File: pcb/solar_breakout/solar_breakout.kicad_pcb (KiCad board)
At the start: 2 copper layers, 21 parts, among them IC1 LTC3105, J1 CONN_01x02, J2 CONN_01x02, J3 CONN_01x02, J4 CONN_01x02, J5 CONN_01x02, J6 CONN_01x02

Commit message: Set up design rules
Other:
- rule pad_to_mask_clearance: 0.051 -> 0
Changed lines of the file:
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@@
     (pad_size 1.524 1.524)
     (pad_drill 0.762)
-    (pad_to_mask_clearance 0.051)
+    (pad_to_mask_clearance 0)
     (solder_mask_min_width 0.25)
     (aux_axis_origin 0 0)

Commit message: First draft of PCB
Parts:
- added REF**: SIL-254P-02, agg:SIL-254P-02, F.Cu at (154.9, 118.3)
- added REF**: SIL-254P-03, agg:SIL-254P-03, F.Cu at (142.1, 119.6)
- added REF**: SIL-254P-02, agg:SIL-254P-02, F.Cu at (158.8, 100.2)
- added REF**: SIL-254P-02, agg:SIL-254P-02, F.Cu at (143.6, 100.2)
- moved D2 154.7 mm to (142.2, 138.4), turned to 90 degrees
- moved J2 148.9 mm to (144.8, 111.1), turned to 270 degrees
- moved C7 146.6 mm to (153.0, 94.0), turned to 180 degrees
- moved L1 145.9 mm to (154.9, 125.7)
- moved J4 144.7 mm to (157.5, 138.4), turned to 270 degrees
- moved IC1 142.9 mm to (149.9, 119.4)
- moved C3 142.8 mm to (153.7, 133.3), turned to 180 degrees
- moved J1 140.1 mm to (149.9, 138.4), turned to 270 degrees
- moved C2 139.8 mm to (147.3, 142.2)
- moved D3 138.2 mm to (142.2, 108.0), turned to 270 degrees
- moved J5 136.4 mm to (149.9, 125.1), turned to 270 degrees
- moved J6 128.5 mm to (163.2, 118.1), turned to 270 degrees
- moved C5 126.8 mm to (146.7, 119.4), turned to 270 degrees
- moved R4 118.7 mm to (154.9, 109.9), turned to 90 degrees
- moved C4 118.0 mm to (146.1, 101.6), turned to 90 degrees
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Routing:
- net /Cap_V: track 0.00 -> 77.3 mm
- net /Panel_V: track 0.00 -> 50.0 mm
- net Net-(C4-Pad1): track 0.00 -> 38.9 mm
- net Net-(IC1-Pad5): track 0.00 -> 26.4 mm
- net Net-(C3-Pad1): track 0.00 -> 22.6 mm
- net Net-(IC1-Pad7): track 0.00 -> 10.1 mm
- net /Array_1_+: track 0.00 -> 7.92 mm
- net /D_anode: track 0.00 -> 5.78 mm
- net /Array_2_+: track 0.00 -> 2.58 mm
- net Net-(C5-Pad1): track 0.00 -> 1.77 mm

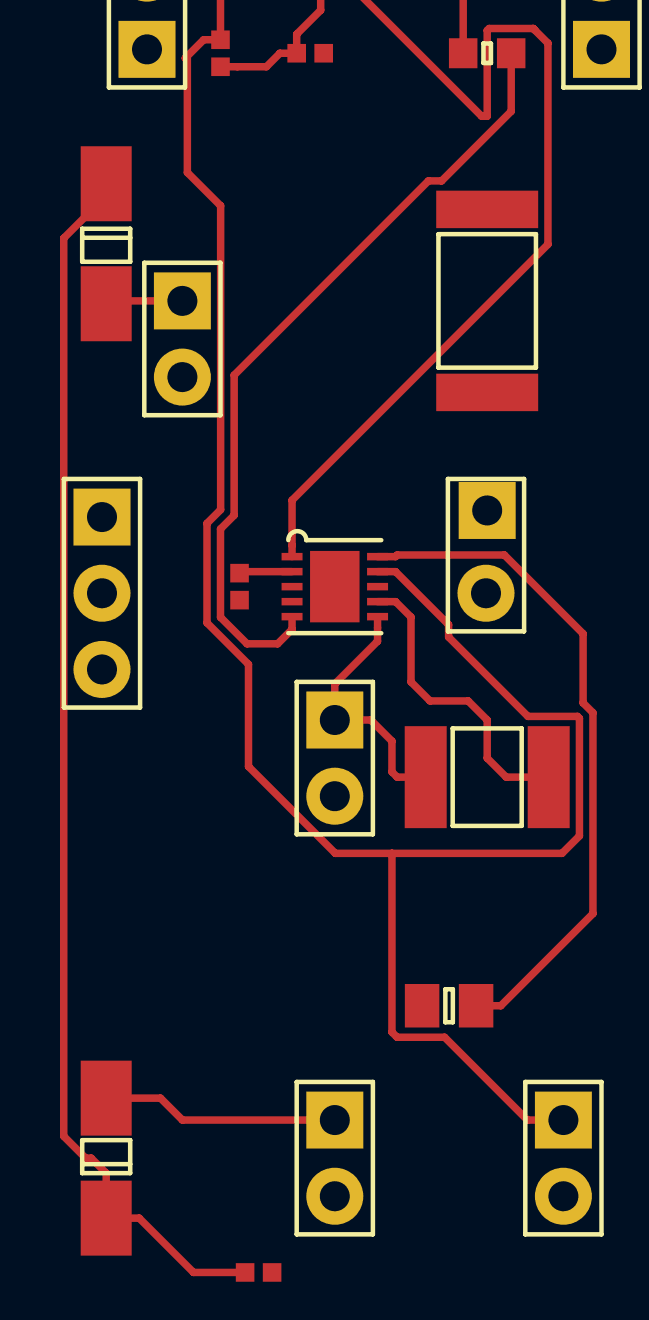
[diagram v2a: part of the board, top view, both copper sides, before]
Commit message: Fix some stuff on pcb (from the Dyson Centre)
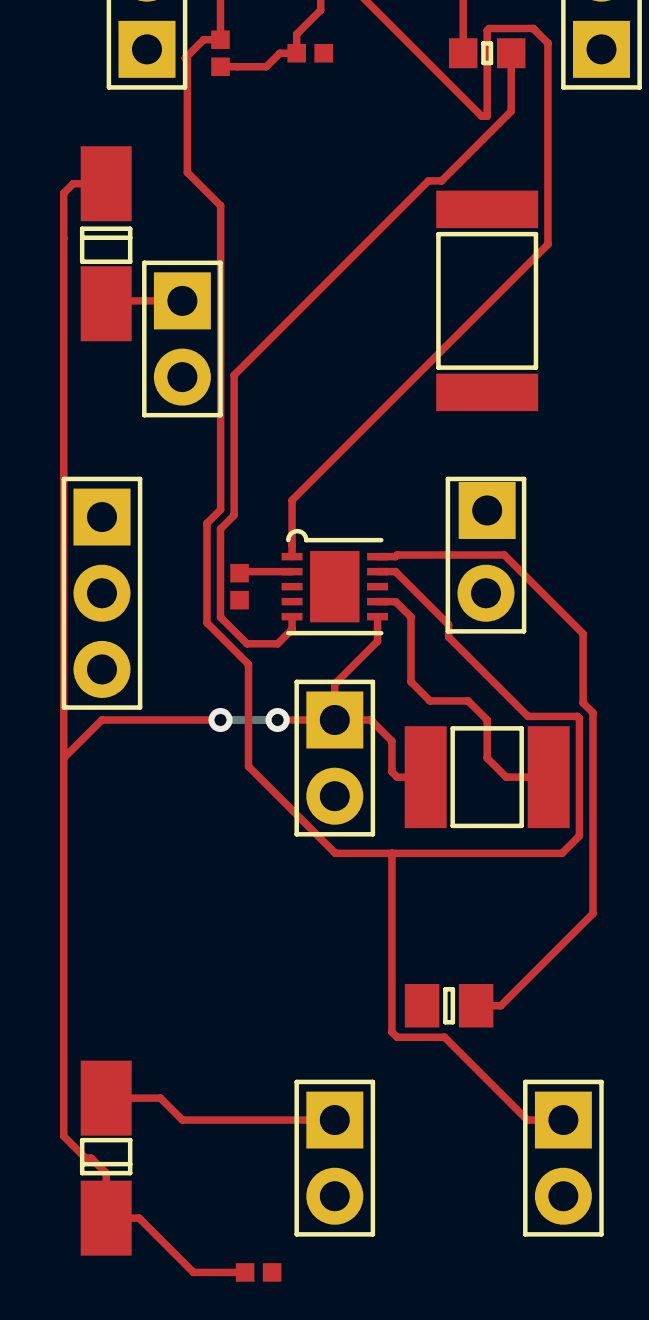
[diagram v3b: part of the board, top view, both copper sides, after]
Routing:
- net /Panel_V: track 50.0 -> 60.6 mm, vias 0 -> 2
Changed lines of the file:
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@@
-(kicad_pcb (version 20171130) (host pcbnew "(6.0.0-rc1-dev-1613-ga55d9819b)")
+(kicad_pcb (version 4) (host pcbnew 4.0.1-stable)
   (general
+    (links 37)
+    (no_connects 17)
+    (area 138.250714 90.315 166.483095 143.919762)
     (thickness 1.6)
     (drawings 0)
-    (tracks 115)
+    (tracks 124)
     (zones 0)
     (modules 25)
@@
     (zone_45_only no)
     (trace_min 0.2)
+    (segment_width 0.2)
+    (edge_width 0.05)
     (via_size 0.8)
     (via_drill 0.4)
@@
     (uvia_min_size 0.2)
     (uvia_min_drill 0.1)
-    (edge_width 0.05)
-    (segment_width 0.2)
     (pcb_text_width 0.3)
     (pcb_text_size 1.5 1.5)
@@
       (layerselection 0x010fc_ffffffff)
       (usegerberextensions false)
-      (usegerberattributes false)
-      (usegerberadvancedattributes false)
-      (creategerberjobfile false)
       (excludeedgelayer true)
       (linewidth 0.100000)
@@
       (hpglpennumber 1)
       (hpglpenspeed 20)
-      (hpglpendiameter 15.000000)
+      (hpglpendiameter 15)
+      (hpglpenoverlay 2)
       (psnegative false)
       (psa4output false)
@@
   (module agg:0402 (layer F.Cu)
     (at 146.685 119.38 270)
-    (fp_text reference C5 (at -1.71 0) (layer F.Fab)
-      (effects (font (size 1 1) (thickness 0.15)))
-    )
-    (fp_text value 4.7u (at 1.71 0) (layer F.Fab)
+    (fp_text reference C5 (at -1.71 0 360) (layer F.Fab)
+      (effects (font (size 1 1) (thickness 0.15)))
+    )
+    (fp_text value 4.7u (at 1.71 0 360) (layer F.Fab)
       (effects (font (size 1 1) (thickness 0.15)))
     )
@@
   (module jerboa:SMA_DIODE (layer F.Cu)
     (at 142.24 107.95 270)
-    (fp_text reference D3 (at -4 0) (layer F.Fab)
-      (effects (font (size 1 1) (thickness 0.15)))
-    )
-    (fp_text value SCHOTTKY (at 4.1 0) (layer F.Fab)
+    (fp_text reference D3 (at -4 0 360) (layer F.Fab)
+      (effects (font (size 1 1) (thickness 0.15)))
+    )
+    (fp_text value SCHOTTKY (at 4.1 0 360) (layer F.Fab)
       (effects (font (size 1 1) (thickness 0.15)))
     )
@@
   (segment (start 154.305 97.155) (end 155.575 97.155) (width 0.25) (layer F.Cu) (net 1))
   (segment (start 154.14 97.32) (end 154.305 97.155) (width 0.25) (layer F.Cu) (net 1))
+  (segment (start 142.24 105.95) (end 141.14 105.95) (width 0.25) (layer F.Cu) (net 3))
+  (segment (start 141.14 105.95) (end 140.824999 106.265001) (width 0.25) (layer F.Cu) (net 3))
+  (segment (start 140.824999 106.265001) (end 140.824999 107.765001) (width 0.25) (layer F.Cu) (net 3))
+  (segment (start 140.824999 107.765001) (end 140.824999 125.095) (width 0.25) (layer F.Cu) (net 3))
+  (segment (start 140.824999 125.095) (end 140.824999 137.700001) (width 0.25) (layer F.Cu) (net 3))
+  (segment (start 146.05 123.825) (end 142.094999 123.825) (width 0.25) (layer F.Cu) (net 3))
+  (segment (start 142.094999 123.825) (end 140.824999 125.095) (width 0.25) (layer F.Cu) (net 3))
+  (segment (start 147.955 123.825) (end 146.05 123.825) (width 0.25) (layer B.Cu) (net 3))
+  (via (at 146.05 123.825) (size 0.8) (drill 0.4) (layers F.Cu B.Cu) (net 3))
+  (segment (start 149.86 123.825) (end 147.955 123.825) (width 0.25) (layer F.Cu) (net 3))
+  (via (at 147.955 123.825) (size 0.8) (drill 0.4) (layers F.Cu B.Cu) (net 3))
   (segment (start 143.34 140.43) (end 142.24 140.43) (width 0.25) (layer F.Cu) (net 3))
   (segment (start 145.15 142.24) (end 143.34 140.43) (width 0.25) (layer F.Cu) (net 3))
@@
   (segment (start 142.24 138.93) (end 142.24 140.43) (width 0.25) (layer F.Cu) (net 3))
   (segment (start 142.24 105.95) (end 142.24 106.35) (width 0.25) (layer F.Cu) (net 3))
-  (segment (start 142.24 106.35) (end 140.824999 107.765001) (width 0.25) (layer F.Cu) (net 3))
-  (segment (start 140.824999 107.765001) (end 140.824999 137.700001) (width 0.25) (layer F.Cu) (net 3))
   (segment (start 140.824999 137.700001) (end 141.554998 138.43) (width 0.25) (layer F.Cu) (net 3))
   (segment (start 141.554998 138.43) (end 141.74 138.43) (width 0.25) (layer F.Cu) (net 3))
@@
   (segment (start 148.03 101.6) (end 147.58 102.05) (width 0.25) (layer F.Cu) (net 5))
   (segment (start 148.59 101.6) (end 148.03 101.6) (width 0.25) (layer F.Cu) (net 5))
-  (segment (start 147.32 96.52) (end 146.94 96.14) (width 0.25) (layer F.Cu) (net 6))
-  (segment (start 147.79 99.06) (end 146.685 99.06) (width 0.25) (layer F.Cu) (net 6))
-  (segment (start 146.685 99.06) (end 146.05 99.695) (width 0.25) (layer F.Cu) (net 6))
-  (segment (start 146.05 99.695) (end 146.05 101.15) (width 0.25) (layer F.Cu) (net 6))
-  (segment (start 147.79 97.32) (end 148.59 96.52) (width 0.25) (layer F.Cu) (net 6))
-  (segment (start 147.79 99.06) (end 147.79 97.32) (width 0.25) (layer F.Cu) (net 6))
-  (segment (start 150.23 96.52) (end 148.59 96.52) (width 0.25) (layer F.Cu) (net 6))
-  (segment (start 148.59 96.52) (end 147.32 96.52) (width 0.25) (layer F.Cu) (net 6))
   (segment (start 150.115 99.06) (end 149.39 99.06) (width 0.25) (layer F.Cu) (net 5))
   (segment (start 154.754999 103.699999) (end 150.115 99.06) (width 0.25) (layer F.Cu) (net 5))
@@
   (segment (start 156.965001 101.264999) (end 156.965001 107.969997) (width 0.25) (layer F.Cu) (net 5))
   (segment (start 156.475001 100.774999) (end 156.965001 101.264999) (width 0.25) (layer F.Cu) (net 5))
+  (segment (start 147.32 96.52) (end 146.94 96.14) (width 0.25) (layer F.Cu) (net 6))
+  (segment (start 147.79 99.06) (end 146.685 99.06) (width 0.25) (layer F.Cu) (net 6))
+  (segment (start 146.685 99.06) (end 146.05 99.695) (width 0.25) (layer F.Cu) (net 6))
+  (segment (start 146.05 99.695) (end 146.05 101.15) (width 0.25) (layer F.Cu) (net 6))
+  (segment (start 147.79 97.32) (end 148.59 96.52) (width 0.25) (layer F.Cu) (net 6))
+  (segment (start 147.79 99.06) (end 147.79 97.32) (width 0.25) (layer F.Cu) (net 6))
+  (segment (start 150.23 96.52) (end 148.59 96.52) (width 0.25) (layer F.Cu) (net 6))
+  (segment (start 148.59 96.52) (end 147.32 96.52) (width 0.25) (layer F.Cu) (net 6))
   (segment (start 151.934999 134.400001) (end 151.765 134.230002) (width 0.25) (layer F.Cu) (net 6))
   (segment (start 153.520001 134.400001) (end 151.934999 134.400001) (width 0.25) (layer F.Cu) (net 6))

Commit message: Work on pcb
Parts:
- removed the REF** at (154.9, 118.3)
- removed the REF** at (143.6, 100.2)
- moved J4 40.7 mm to (143.6, 100.2), turned to 90 degrees
- moved J6 13.9 mm to (151.1, 111.1), turned to 90 degrees
- moved C2 12.3 mm to (146.1, 130.0), turned to 90 degrees
- moved J1 9.61 mm to (148.6, 128.9)
- moved D2 9.61 mm to (143.5, 128.9)
- moved J5 8.44 mm to (154.9, 118.3)
- moved C3 3.20 mm to (154.0, 130.2)
- moved L1 1.27 mm to (153.7, 125.7)
- moved C1 0.63 mm to (154.9, 99.7)
- moved J2 0.63 mm to (145.4, 111.1)
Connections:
- J5 pad 2: GND -> /Cap_V
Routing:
- net GND: track 0.00 -> 16.8 mm, vias 0 -> 5
- net /Panel_V: track 60.6 -> 73.3 mm
- net /Cap_V: track 77.3 -> 70.7 mm
- net Net-(IC1-Pad5): track 26.4 -> 31.4 mm
- net Net-(J6-Pad1): track 0.00 -> 4.02 mm
- net Net-(C4-Pad1): track 38.9 -> 41.5 mm
- net /Array_1_+: track 7.92 -> 5.38 mm
- net Net-(IC1-Pad7): track 10.1 -> 8.60 mm
- net Net-(C3-Pad1): track 22.6 -> 23.9 mm
- added copper zone on B.Cu, net GND

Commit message: Add more stuff to pcb
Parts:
- moved R1 1.42 mm to (155.6, 102.9), turned to 90 degrees
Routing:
- net Net-(C4-Pad1): track 41.5 -> 37.2 mm
- net /D_anode: track 5.78 -> 7.41 mm
- net Net-(IC1-Pad5): track 31.4 -> 29.9 mm
- net /Cap_V: track 70.7 -> 69.5 mm
- net Net-(C3-Pad1): track 23.9 -> 23.2 mm

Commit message: Update pcb
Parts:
- R1: value R -> 30k
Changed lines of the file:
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@@
       (effects (font (size 1 1) (thickness 0.15)))
     )
-    (fp_text value R (at 2.225 0 180) (layer F.Fab)
+    (fp_text value 30k (at 2.225 0 180) (layer F.Fab)
       (effects (font (size 1 1) (thickness 0.15)))
     )

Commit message: Update PCB
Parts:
- added G***: LOGO, jerboa:cusf_logo, B.Cu at (158.6, 123.1)
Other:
- board text added: "+"
- board text added: "-"
- board text added: "ARRAY1"
- board text added: "ARRAY2"
- board text added: "CAP"
- board text added: "JUMPER"
- board text added: "Jerboa Solar"
- board text added: "RPR"
- board text added: "VCAP"
- board text added: "VSOLAR"
- board text added: "Vout"
- board text added: "http://www.cusf.co.uk/"

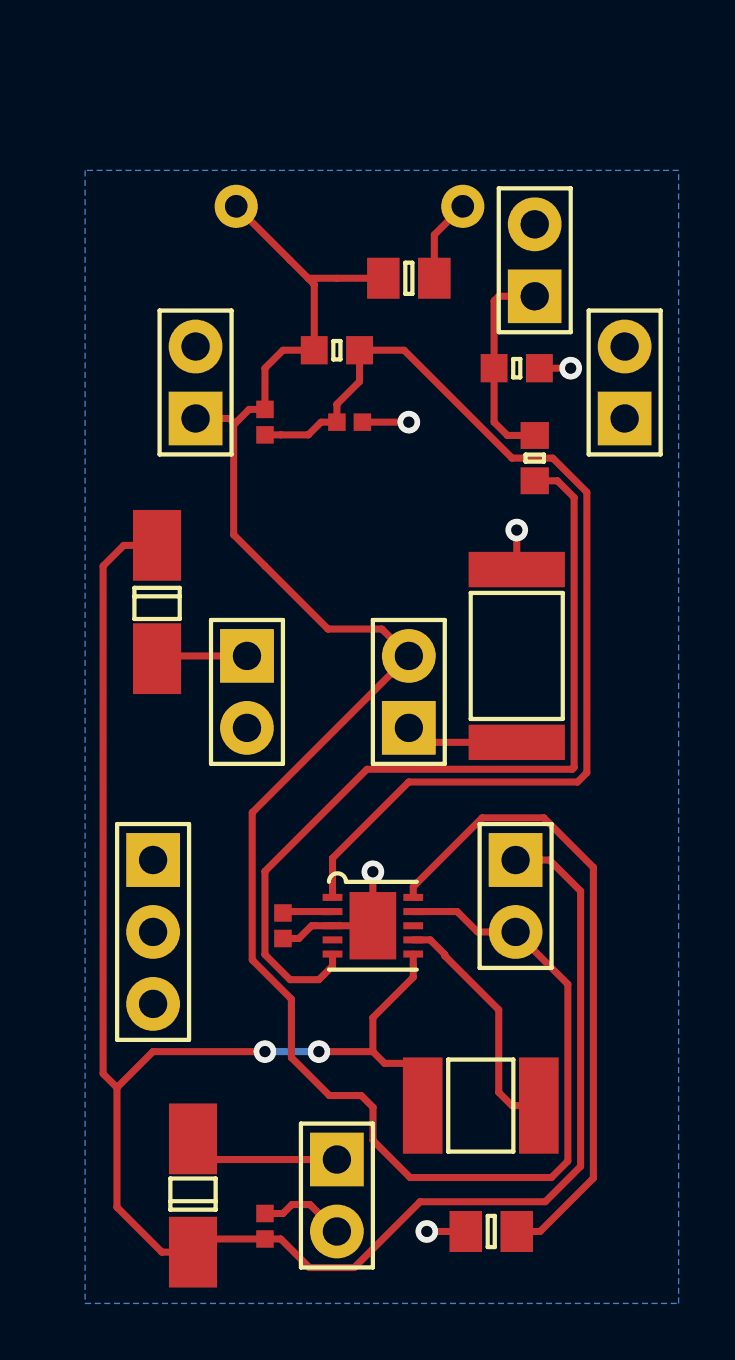
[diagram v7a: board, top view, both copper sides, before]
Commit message: Do checks on PCB and add edge cuts
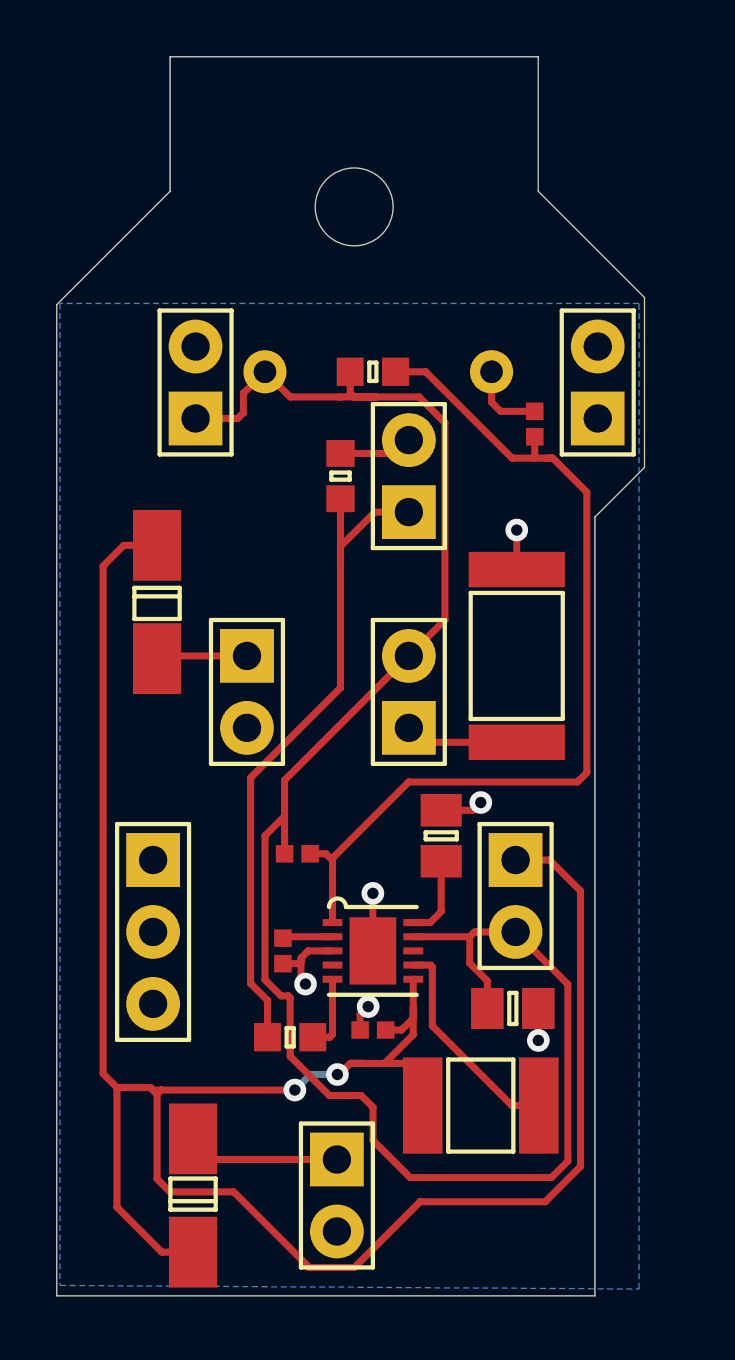
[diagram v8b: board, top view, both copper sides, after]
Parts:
- removed the G*** at (158.6, 123.1)
- added G***: LOGO, jerboa:cusf_logo_small, B.Cu at (148.5, 117.7)
- added REF**: M2.5_HOLE, agg:M2.5_HOLE, F.Cu at (149.2, 94.0)
- moved C6 26.0 mm to (154.8, 122.3)
- moved R1 22.2 mm to (146.9, 123.3), turned to 180 degrees
- moved C4 15.3 mm to (147.2, 116.8), turned to 180 degrees
- moved C3 14.1 mm to (152.3, 116.2), turned to 90 degrees
- moved J3 8.82 mm to (151.1, 103.5)
- moved C2 7.91 mm to (149.9, 123.1), turned to 180 degrees
- moved C1 7.30 mm to (148.7, 103.5), turned to 90 degrees
- moved R3 6.54 mm to (155.6, 101.7), turned to 90 degrees
- moved C7 5.93 mm to (154.1, 99.8)
- moved R2 1.48 mm to (149.9, 99.8)
- moved REF** 0.95 mm to (157.8, 100.2)
- moved C5 0.89 mm to (146.7, 120.3)
- moved IC1 0.89 mm to (149.9, 120.3)
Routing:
- net Net-(IC1-Pad5): track 29.9 -> 2.69 mm
- net Net-(C3-Pad1): track 23.2 -> 3.45 mm
- net /D_anode: track 7.41 -> 24.8 mm
- net /Panel_V: track 73.8 -> 81.0 mm
- net Net-(C4-Pad1): track 37.2 -> 33.2 mm
- net /Cap_V: track 69.2 -> 67.1 mm
- net GND: track 16.8 -> 15.1 mm, vias 5 -> 6
- net Net-(IC1-Pad7): track 8.60 -> 7.71 mm
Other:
- board outline added: 20.8 x 43.7 mm
- board text added: "Feb 2019"
- board text added: "Joel Mayer"
- board text added: "VOUT"
- board text added: "Version 1"
- board text removed: "Vout"
